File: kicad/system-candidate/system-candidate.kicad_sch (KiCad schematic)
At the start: 263 parts, among them J1 691137710002 2P 5.00mm, J2 Auxiliary 12V, J3 Differential audio, J301 T1_SECONDARY, J4 Control 2x4: 3V3 RESET FAULT 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, J401 START_BUTTON, J5 B2P-VH(LF)(SN), J6 GND braid solder bond - NO mo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, J7 B7B-XH-A(LF)(SN), J8 FAN 12V, K501 G6K-2F DC12, Q501 MMBT3904, Q502 MMBT3904, Q601 BCP56, Q602 BCP53, Q603 BSS138, Q701 BSS138, Q702 BSS138, Q703 BSS138, Q704 BSS138, Q705 BSS138, Q706 BSS138, Q707 AO3400A, U1 TPA3255DDV, U2 OPA1656ID, U3 OPA1656ID, U302 LM5164DDA, U303 TPS3700DDC, U401 LP2985-33, U402 TPS3808G33, U403 TPS3808G33, U404 TPS3808G33, U405 74LVC1G14, U406 74LVC2G74, U407 74LVC2G74, U408 74LVC1G32, U409 74LVC1G07, U410 74LVC1G08, U411 74LVC1G06, U412 TPS3700DDC, U413 TPS3700DDC, U414 TPS3808G33, U415 74LVC1G08, U416 TPS3808G33, U417 74LVC2G74, U418 74LVC1G32, U419 74LVC1G07, U501 TPS3700DDC, U502 TPS3700DDC, U503 TMUX6219, U504 TPS3700DDC

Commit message: fix(pcb): close routing and verify nominal fit
Correct TPA placement and TP127/R506 connectivity.\nPreserve OEM fit assumptions and explicit fabrication gates.\nSync documentation, renders, tasks and GitHub mirrors.\n\nValidate ERC/DRC/parity and 138 local tests.\n\nRefs #3, #7, #8, #10, #11
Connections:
- net INA_UV: no longer C503.1, D503.3 (K), R505.1, R517.2, TP127.1, U1.5 (INPUT_A)
- new net INPUT_A_AC: C503.1, D503.3 (K), R505.1, R517.2, TP127.1, U1.5 (INPUT_A)
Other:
- moved on the sheet: R107, R108, TP127

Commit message: fix(pcb): reconcile purchasing codes and add verified studio drafts
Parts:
- C14, C15: MPN UHE1J152MHD -> UHE1J681MHD
- J5: MPN 691137710002 -> B2P-VH(LF)(SN); Manufacturer Wurth Elektronik -> JST
- R101: MPN CRCW06031K00FKEA -> CRCW08051K00FKEA; Manufacturer (none) -> Vishay
- R102: MPN CRCW0603100KFKEA -> CRCW0805100KFKEA; Manufacturer (none) -> Vishay
- R310: MPN RG1608P-1053-B-T5 (TI Table 7-1); FSW 300 kHz -> RT0603BRD07100KL; Manufacturer (none) -> YAGEO

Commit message: fix(eda): align source notes and keep the whole board framed
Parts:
- C14, C15: Source Nichicon UHE CAT.8100M p.1/p.6: UHE1J152MHD 1500uF 63V D18 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 -> Nichicon UHE CAT.8100M: UHE1J681MHD 680uF 63V D12.5x40 P5; 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
- J5: Source WE WR-TBL1377 rev001.003 2021-07-30 p.1-2: pitch5.00 NOT5.0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 -> JST VH eVH-new p.3: B2P-VH(LF)(SN), 2 circuits, pitch3.96mm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

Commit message: feat(bom): close remaining 190 purchase selections
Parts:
- C1: SelectionNotes (none) -> WE WCAP-ATG5 rev1.0 2014-11-11 p.1: 470uF 35V D10 H16+1.5 P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; SelectionStatus Selected for engineering validation; NO procurement/release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 -> MPN SELECTED; supply/DFM/bench release pending
- C10, C11, C12, C13, C16, C17, C18, C19, C2, C20, C21, C24, C25, C28, C29, C3, C4, C5, C6, C7, C8, C9, J2: SelectionNotes (none) -> TI SLOU441 July2016 Table8 p.14-16; nominal package geometr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; SelectionStatus Selected for engineering validation; NO procurement/release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 -> MPN SELECTED; supply/DFM/bench release pending
- C107, C108: MPN TBD -> C0805C104K5RACTU; Manufacturer (none) -> KEMET; SelectionNotes (none) -> 100nF; 50V; X7R; 10%; 0805; SelectionStatus CANDIDATE; NOT PULSE/ESR/POWER-OFF/FIT QUALIFIED -> MPN SELECTED; supply/DFM/bench release pending
- C109: footprint Capacitor_THT:C_Rect_L7.2mm_W5.5mm_P5.00mm_FKS2_FKP2_MKS2_MKP2 -> Capacitor_THT:C_Rect_L7.2mm_W7.2mm_P5.00mm_FKS2_FKP2_MKS2_MKP2; MPN Film 2.2 uF >=63 V, P5 mm (WIMA MKS2 class); MPN at BOM -> MKS2C042201K00JSSD; Manufacturer (none) -> WIMA; SelectionNotes (none) -> 2.2uF; 63V; 5%; PET film; W7.2 H13 L7.2mm; pitch5; body foo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; SelectionStatus STUDY; passives/interfaces not selected -> MPN SELECTED; supply/DFM/bench release pending
- C14, C15: SelectionNotes (none) -> Nichicon UHE CAT.8100M: UHE1J681MHD 680uF 63V D12.5x40 P5; 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; SelectionStatus Selected for engineering validation; NO procurement/release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 -> MPN SELECTED; supply/DFM/bench release pending
- C201, C202: Manufacturer (none) -> Wurth Elektronik; SelectionNotes (none) -> 470uF; 35V; D10x16; pitch5; unchanged selected core capacit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; SelectionStatus CANDIDATE; NOT PULSE/ESR/POWER-OFF/FIT QUALIFIED -> MPN SELECTED; supply/DFM/bench release pending
- C203: Manufacturer (none) -> WIMA; SelectionNotes (none) -> 1uF; 63V; 5%; PP film; W11 H21 L7.2mm; pitch5; SelectionStatus CANDIDATE; NOT PULSE/ESR/POWER-OFF/FIT QUALIFIED -> MPN SELECTED; supply/DFM/bench release pending
- C22, C23, C26, C27: SelectionNotes (none) -> WIMA MKP2 03.26 p.38-39: 470nF 100V, W8.5 H14 L7.2 PCM5; J 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; SelectionStatus Selected for engineering validation; NO procurement/release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 -> MPN SELECTED; supply/DFM/bench release pending
- C301, C302: MPN Rubycon 63USC4700MEFCSN30X30 (LCSC C1498587): 4700 uF/63 V,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 -> 63USC4700MEFCSN30X30; Manufacturer (none) -> Rubycon; SelectionNotes (none) -> 4700uF; 63V; D30x30; pitch10; 3.49Arms/120Hz; total with C1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; SelectionStatus STUDY; passives/interfaces not selected -> MPN SELECTED; supply/DFM/bench release pending; Source D-021/D-020 captures; see docs/power-d021.md and docs/seq-d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 -> https://www.rubycon.co.jp/wp-content/uploads/catalog-alumin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
- C310, C311: MPN CGA6N3X7R2A225K230AB (TI Table 7-1) -> CGA6N3X7R2A225K230AB; Manufacturer (none) -> TDK; SelectionNotes (none) -> 2.2uF; 100V; X7R; 1210; TI Table7-1; effective capacitance 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; SelectionStatus STUDY; passives/interfaces not selected -> MPN SELECTED; supply/DFM/bench release pending
- C312: MPN GCM155R71H222KA37D (TI Table 7-1); 1.5-2.5 nF abs range -> GCM155R71H222KA37D; Manufacturer (none) -> Murata; SelectionNotes (none) -> 2.2nF; 50V; X7R; 0402; 10%; within TI bootstrap1.5-2.5nF at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; SelectionStatus STUDY; passives/interfaces not selected -> MPN SELECTED; supply/DFM/bench release pending
- C313: MPN CGA3E2X7R2A332K080AA (TI Table 7-1); CA -> CGA3E2X7R2A332K080AA; Manufacturer (none) -> TDK; SelectionNotes (none) -> 3.3nF; 100V; X7R; 0603; TI Table7-1; SelectionStatus STUDY; passives/interfaces not selected -> MPN SELECTED; supply/DFM/bench release pending
- C314: MPN C0603C560J5GACTU (TI Table 7-1); CB -> C0603C560J5GACTU; Manufacturer (none) -> KEMET; SelectionNotes (none) -> 56pF; 50V; C0G; 5%; 0603; TI Table7-1; SelectionStatus STUDY; passives/interfaces not selected -> MPN SELECTED; supply/DFM/bench release pending
- C315, C316: MPN TMK325B7226KMHT (TI Table 7-1) -> TMK325B7226KMHT; Manufacturer (none) -> Taiyo Yuden; SelectionNotes (none) -> 22uF; 25V; X7R; 1210; TI Table7-1; SelectionStatus STUDY; passives/interfaces not selected -> MPN SELECTED; supply/DFM/bench release pending
- C320: MPN TBD: X7R >=25 V (SBVS187G p.4 VDD bypass) -> C0603C104K5RACTU; Manufacturer (none) -> KEMET; SelectionNotes (none) -> 100nF; 50V; X7R; 10%; 0603; SelectionStatus STUDY; passives/interfaces not selected -> MPN SELECTED; supply/DFM/bench release pending
- C401: MPN TBD: X7R >=25 V; CIN >=1 uF (SLVS522S Table 4-1) -> GRM188R71E105KA12D; Manufacturer (none) -> Murata; SelectionNotes (none) -> 1uF; 25V; X7R; 10%; 0603; C401 input at12V: bias derating a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; SelectionStatus STUDY; passives/interfaces not selected -> MPN SELECTED; supply/DFM/bench release pending
- C402: MPN TBD: X7R; CBYPASS 10 nF (SLVS522S) -> 06031C103KAT2A; Manufacturer (none) -> KYOCERA AVX; SelectionNotes (none) -> 10nF; 100V; X7R; 10%; 0603; same as selected C25/C29; SelectionStatus STUDY; passives/interfaces not selected -> MPN SELECTED; supply/DFM/bench release pending
- C403: MPN TBD: X7R, >=1 uF effective, ESR <=1 ohm new die -> GRM188Z71C225KE43D; Manufacturer (none) -> Murata; SelectionNotes (none) -> 2.2uF; 16V; X7R(Murata); 10%; 0603; TI EVM C118; LP2985 out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; SelectionStatus STUDY; passives/interfaces not selected -> MPN SELECTED; supply/DFM/bench release pending
- C404: MPN TBD: C0G/X7R low leakage; CT 180 nF => 0.62-1.44 s -> GRM188R71E184KA88D; Manufacturer (none) -> Murata; SelectionNotes (none) -> 180nF; 25V; X7R; 10%; 0603; CT at low bias; specified timin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; SelectionStatus STUDY; passives/interfaces not selected -> MPN SELECTED; supply/DFM/bench release pending
- C405: MPN TBD: X7R; release tau ~110 ms -> GRM188R71E105KA12D; Manufacturer (none) -> Murata; SelectionNotes (none) -> 1uF; 25V; X7R; 10%; 0603; C401 input at12V: bias derating a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; SelectionStatus STUDY; passives/interfaces not selected -> MPN SELECTED; supply/DFM/bench release pending
- C406: MPN TBD: X7R >=10 V; U402 -> C0603C104K5RACTU; Manufacturer (none) -> KEMET; SelectionNotes (none) -> 100nF; 50V; X7R; 10%; 0603; SelectionStatus STUDY; passives/interfaces not selected -> MPN SELECTED; supply/DFM/bench release pending
- C407: MPN TBD: X7R >=10 V; U403 -> C0603C104K5RACTU; Manufacturer (none) -> KEMET; SelectionNotes (none) -> 100nF; 50V; X7R; 10%; 0603; SelectionStatus STUDY; passives/interfaces not selected -> MPN SELECTED; supply/DFM/bench release pending
- C408: MPN TBD: X7R >=10 V; U404 -> C0603C104K5RACTU; Manufacturer (none) -> KEMET; SelectionNotes (none) -> 100nF; 50V; X7R; 10%; 0603; SelectionStatus STUDY; passives/interfaces not selected -> MPN SELECTED; supply/DFM/bench release pending
- C409: MPN TBD: X7R >=10 V; U405 -> C0603C104K5RACTU; Manufacturer (none) -> KEMET; SelectionNotes (none) -> 100nF; 50V; X7R; 10%; 0603; SelectionStatus STUDY; passives/interfaces not selected -> MPN SELECTED; supply/DFM/bench release pending
- C410: MPN TBD: X7R >=10 V; U406 -> C0603C104K5RACTU; Manufacturer (none) -> KEMET; SelectionNotes (none) -> 100nF; 50V; X7R; 10%; 0603; SelectionStatus STUDY; passives/interfaces not selected -> MPN SELECTED; supply/DFM/bench release pending
- C411: MPN TBD: X7R >=10 V; U407 -> C0603C104K5RACTU; Manufacturer (none) -> KEMET; SelectionNotes (none) -> 100nF; 50V; X7R; 10%; 0603; SelectionStatus STUDY; passives/interfaces not selected -> MPN SELECTED; supply/DFM/bench release pending
- C412: MPN TBD: X7R >=10 V; U408 -> C0603C104K5RACTU; Manufacturer (none) -> KEMET; SelectionNotes (none) -> 100nF; 50V; X7R; 10%; 0603; SelectionStatus STUDY; passives/interfaces not selected -> MPN SELECTED; supply/DFM/bench release pending
- C413: MPN TBD: X7R >=10 V; U409 -> C0603C104K5RACTU; Manufacturer (none) -> KEMET; SelectionNotes (none) -> 100nF; 50V; X7R; 10%; 0603; SelectionStatus STUDY; passives/interfaces not selected -> MPN SELECTED; supply/DFM/bench release pending
- C414: MPN TBD: X7R >=10 V; U410 -> C0603C104K5RACTU; Manufacturer (none) -> KEMET; SelectionNotes (none) -> 100nF; 50V; X7R; 10%; 0603; SelectionStatus STUDY; passives/interfaces not selected -> MPN SELECTED; supply/DFM/bench release pending
- C415: MPN TBD: X7R >=10 V; U411 -> C0603C104K5RACTU; Manufacturer (none) -> KEMET; SelectionNotes (none) -> 100nF; 50V; X7R; 10%; 0603; SelectionStatus STUDY; passives/interfaces not selected -> MPN SELECTED; supply/DFM/bench release pending
- C416: MPN TBD: X7R >=25 V; U412 VDD -> C0603C104K5RACTU; Manufacturer (none) -> KEMET; SelectionNotes (none) -> 100nF; 50V; X7R; 10%; 0603; SelectionStatus STUDY; passives/interfaces not selected -> MPN SELECTED; supply/DFM/bench release pending
- C417: MPN TBD: X7R >=25 V; U413 VDD -> C0603C104K5RACTU; Manufacturer (none) -> KEMET; SelectionNotes (none) -> 100nF; 50V; X7R; 10%; 0603; SelectionStatus STUDY; passives/interfaces not selected -> MPN SELECTED; supply/DFM/bench release pending
- C418: MPN TBD: X7R >=10 V; U414 -> C0603C104K5RACTU; Manufacturer (none) -> KEMET; SelectionNotes (none) -> 100nF; 50V; X7R; 10%; 0603; SelectionStatus STUDY; passives/interfaces not selected -> MPN SELECTED; supply/DFM/bench release pending
- C419: MPN TBD: X7R >=10 V; U415 -> C0603C104K5RACTU; Manufacturer (none) -> KEMET; SelectionNotes (none) -> 100nF; 50V; X7R; 10%; 0603; SelectionStatus STUDY; passives/interfaces not selected -> MPN SELECTED; supply/DFM/bench release pending
- C420: MPN TBD: X7R >=10 V; U416 -> C0603C104K5RACTU; Manufacturer (none) -> KEMET; SelectionNotes (none) -> 100nF; 50V; X7R; 10%; 0603; SelectionStatus STUDY; passives/interfaces not selected -> MPN SELECTED; supply/DFM/bench release pending
- C421: MPN TBD: X7R >=10 V; U417 -> C0603C104K5RACTU; Manufacturer (none) -> KEMET; SelectionNotes (none) -> 100nF; 50V; X7R; 10%; 0603; SelectionStatus STUDY; passives/interfaces not selected -> MPN SELECTED; supply/DFM/bench release pending
- C422: MPN TBD: X7R >=10 V; U418 -> C0603C104K5RACTU; Manufacturer (none) -> KEMET; SelectionNotes (none) -> 100nF; 50V; X7R; 10%; 0603; SelectionStatus STUDY; passives/interfaces not selected -> MPN SELECTED; supply/DFM/bench release pending
- C423: MPN TBD: X7R >=10 V; U419 -> C0603C104K5RACTU; Manufacturer (none) -> KEMET; SelectionNotes (none) -> 100nF; 50V; X7R; 10%; 0603; SelectionStatus STUDY; passives/interfaces not selected -> MPN SELECTED; supply/DFM/bench release pending
- C503, C504: MPN TBD: C0G/NP0 >=50 V -> C0603C472J5GACTU; Manufacturer (none) -> KEMET; SelectionNotes (none) -> 4.7nF; 50V; C0G; 5%; 0603; SelectionStatus STUDY; passives/interfaces not selected -> MPN SELECTED; supply/DFM/bench release pending
- C505: MPN TBD: X7R >=25 V; U503 VDD (SCDS420E Table 4-1) -> C0603C104K5RACTU; Manufacturer (none) -> KEMET; SelectionNotes (none) -> 100nF; 50V; X7R; 10%; 0603; SelectionStatus STUDY; passives/interfaces not selected -> MPN SELECTED; supply/DFM/bench release pending
- C506: MPN TBD: X7R >=25 V; U501 VDD -> C0603C104K5RACTU; Manufacturer (none) -> KEMET; SelectionNotes (none) -> 100nF; 50V; X7R; 10%; 0603; SelectionStatus STUDY; passives/interfaces not selected -> MPN SELECTED; supply/DFM/bench release pending
- C507: MPN TBD: X7R >=25 V; U502 VDD -> C0603C104K5RACTU; Manufacturer (none) -> KEMET; SelectionNotes (none) -> 100nF; 50V; X7R; 10%; 0603; SelectionStatus STUDY; passives/interfaces not selected -> MPN SELECTED; supply/DFM/bench release pending
- C508: MPN TBD: X7R >=25 V; U504 VDD -> C0603C104K5RACTU; Manufacturer (none) -> KEMET; SelectionNotes (none) -> 100nF; 50V; X7R; 10%; 0603; SelectionStatus STUDY; passives/interfaces not selected -> MPN SELECTED; supply/DFM/bench release pending
- C509, C511: MPN TBD: X7R >=16 V; UV tap filter -> C0603C334K4RACTU; Manufacturer (none) -> KEMET; SelectionNotes (none) -> 330nF; 16V; X7R; 10%; 0603; window tap <1V; SelectionStatus STUDY; passives/interfaces not selected -> MPN SELECTED; supply/DFM/bench release pending
- C510, C512: MPN TBD: X7R >=16 V; OV tap filter -> CC0603KRX7R8BB684; Manufacturer (none) -> YAGEO; SelectionNotes (none) -> 680nF; 25V; X7R; 10%; 0603; window tap <1V; SelectionStatus STUDY; passives/interfaces not selected -> MPN SELECTED; supply/DFM/bench release pending
- C601, C604: MPN X7R 1206 >=25 V; MPN at BOM -> C3216X7R1E106K160AB; Manufacturer (none) -> TDK; SelectionNotes (none) -> 10uF; 25V; X7R; 10%; 1206; OEM +/-15V interface bypass; SelectionStatus STUDY; passives/interfaces not selected -> MPN SELECTED; supply/DFM/bench release pending
- C602, C605: MPN X7R 0603 50 V -> C0603C104K5RACTU; Manufacturer (none) -> KEMET; SelectionNotes (none) -> 100nF; 50V; X7R; 10%; 0603; SelectionStatus STUDY; passives/interfaces not selected -> MPN SELECTED; supply/DFM/bench release pending
- C603: MPN Nichicon UHE1J121MPD 120 uF/63 V 8x20 (CAT.8100M) -> UHE1J121MPD; Manufacturer (none) -> Nichicon; SelectionNotes (none) -> 120uF; 63V; D8x20; pitch3.5; SelectionStatus STUDY; passives/interfaces not selected -> MPN SELECTED; supply/DFM/bench release pending
- D201: Manufacturer (none) -> Vishay; SelectionNotes (none) -> 1000V; 1A; DO41 axial; polarity per footprint cathode1; SelectionStatus CANDIDATE; NOT PULSE/ESR/POWER-OFF/FIT QUALIFIED -> MPN SELECTED; supply/DFM/bench release pending
- D301, D302: MPN P600J (Diodes Inc./Vishay), R-6 axial: 600 V, 6 A, IFSM 400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 -> P600J-E3/54; Manufacturer (none) -> Vishay; SelectionNotes (none) -> 600V; 6A; IFSM400A; P600/R6 axial; CT rectifier; manual lea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; SelectionStatus STUDY; passives/interfaces not selected -> MPN SELECTED; supply/DFM/bench release pending
- D303: MPN Littelfuse SMCJ51A: VWM 51.0 V, Vc 82.4 V @IPP 18.2 A, PPP 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 -> SMCJ51A; Manufacturer (none) -> Littelfuse; SelectionNotes (none) -> 51V standoff; 1500W10/1000us; Vclamp82.4V; not sustained ra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; SelectionStatus STUDY; passives/interfaces not selected -> MPN SELECTED; supply/DFM/bench release pending
- D501: MPN 1N4148W-7-F (Diodes DS30086) -> 1N4148W-7-F; Manufacturer (none) -> Diodes Incorporated; SelectionNotes (none) -> SOD123; fast signal diode; SelectionStatus STUDY; passives/interfaces not selected -> MPN SELECTED; supply/DFM/bench release pending
- D502: MPN BZT52C15-7-F (Diodes DS18004): 13.8-15.6 V; faster release -> BZT52C15-7-F; Manufacturer (none) -> Diodes Incorporated; SelectionNotes (none) -> 15V; SOD123; 13.8-15.6V at5mA; SelectionStatus STUDY; passives/interfaces not selected -> MPN SELECTED; supply/DFM/bench release pending
- D503, D504: MPN BAT54-7-F (Diodes DS11005 Rev.34) -> BAT54-7-F; Manufacturer (none) -> Diodes Incorporated; SelectionNotes (none) -> 30V; SOT23; single Schottky; pin1 A pin3 K; SelectionStatus STUDY; passives/interfaces not selected -> MPN SELECTED; supply/DFM/bench release pending
- D601: MPN Diodes BZT52C16 (DS18004): 15.3-17.1 V @5 mA -> BZT52C16-7-F; Manufacturer (none) -> Diodes Incorporated; SelectionNotes (none) -> 16V; SOD123; 15.3-17.1V at5mA; SelectionStatus STUDY; passives/interfaces not selected -> MPN SELECTED; supply/DFM/bench release pending
- D602, D603: MPN S1M 1000 V 1 A SMA (Vishay/onsemi); light load -> S1M-E3/61T; Manufacturer (none) -> Vishay; SelectionNotes (none) -> 1000V; 1A; SMA/DO214AC; cathode1; light-load rectification/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; SelectionStatus STUDY; passives/interfaces not selected -> MPN SELECTED; supply/DFM/bench release pending
- D604: MPN Diodes BZT52C16 (DS18004) -> BZT52C16-7-F; Manufacturer (none) -> Diodes Incorporated; SelectionNotes (none) -> 16V; SOD123; 15.3-17.1V at5mA; SelectionStatus STUDY; passives/interfaces not selected -> MPN SELECTED; supply/DFM/bench release pending
- D701, D702, D703, D704, D705, D706: MPN Green 0805 LED (e.g. Lite-On LTST-C171GKT) -> LTST-C171GKT; Manufacturer (none) -> Lite-On; SelectionNotes (none) -> green LED; 0805; polarity pin1 cathode; resistive current l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; SelectionStatus STUDY; passives/interfaces not selected -> MPN SELECTED; supply/DFM/bench release pending
- D707: MPN S1M flyback across the fan -> S1M-E3/61T; Manufacturer (none) -> Vishay; SelectionNotes (none) -> 1000V; 1A; SMA/DO214AC; cathode1; light-load rectification/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; SelectionStatus STUDY; passives/interfaces not selected -> MPN SELECTED; supply/DFM/bench release pending
- F301: MPN Littelfuse 02186.3MXP, 218 series T 6.3 A 5x20 mm, in Schur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 -> 0031.8201; Manufacturer (none) -> Schurter; SelectionNotes (none) -> PCB fuse holder for5x20; P22.5mm; separate fuse F301-FUSE i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; SelectionStatus STUDY; passives/interfaces not selected -> MPN SELECTED; supply/DFM/bench release pending
- J1: SelectionNotes (none) -> WE WR-TBL1377 rev001.003 2021-07-30 p.1-2: pitch5.00 NOT5.0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; SelectionStatus Selected for engineering validation; NO procurement/release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 -> MPN SELECTED; supply/DFM/bench release pending
- J301: MPN JST B3P-VH(LF)(SN) header 3 pos 3.96 mm; mates OEM T1 harne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 -> B3P-VH(LF)(SN); Manufacturer (none) -> JST; SelectionNotes (none) -> 3way; 3.96mm; CT T1 OEM harness, never bridge red-red; SelectionStatus STUDY; passives/interfaces not selected -> MPN SELECTED; supply/DFM/bench release pending
- J401: MPN TBD: panel momentary switch harness; location/mechanics not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 -> PBC02SAAN; Manufacturer (none) -> Sullins Connector Solutions; SelectionNotes (none) -> 2pin straight header; P2.54mm; external momentary NO switch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; SelectionStatus STUDY; passives/interfaces not selected -> MPN SELECTED; supply/DFM/bench release pending
- J5: SelectionNotes (none) -> JST VH eVH-new p.3: B2P-VH(LF)(SN), 2 circuits, pitch3.96mm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; SelectionStatus Selected for engineering validation; NO procurement/release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 -> MPN SELECTED; supply/DFM/bench release pending
- J7: MPN JST B7B-XH-A(LF)(SN), 2.5 mm: mates OEM 7-way preamp harnes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 -> B7B-XH-A(LF)(SN); Manufacturer (none) -> JST; SelectionNotes (none) -> 7way; 2.5mm; mates OEM P101 harness, pinout per current des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; SelectionStatus STUDY; passives/interfaces not selected -> MPN SELECTED; supply/DFM/bench release pending
- J8: MPN JST B2B-XH-A(LF)(SN); fan <= 200 mA -> B2B-XH-A(LF)(SN); Manufacturer (none) -> JST; SelectionNotes (none) -> 2way; 2.5mm; fan<=200mA; SelectionStatus STUDY; passives/interfaces not selected -> MPN SELECTED; supply/DFM/bench release pending
- JP701: MPN 2.54 mm header + jumper: 1-2 ON, 2-3 OTW -> PBC03SAAN; Manufacturer (none) -> Sullins Connector Solutions; SelectionNotes (none) -> 3pin straight header; P2.54mm; shunt separate accessory; 1-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; SelectionStatus STUDY; passives/interfaces not selected -> MPN SELECTED; supply/DFM/bench release pending
- K501: MPN G6K-2F DC12 (Omron K106-E1-11 p.2-3: 1315 ohm, 3 ms operate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 -> G6K-2F DC12; Manufacturer (none) -> Omron; SelectionNotes (none) -> 12V monostable DPDT; SMD; 1315ohm; operate/release3ms max; 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; SelectionStatus STUDY; passives/interfaces not selected -> MPN SELECTED; supply/DFM/bench release pending
- L1, L2: SelectionNotes (none) -> WE 006.000 2025-07-08 p.1: 10uH/16A/22A typ/8.76mOhm max; s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; SelectionStatus Selected for engineering validation; NO procurement/release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 -> MPN SELECTED; supply/DFM/bench release pending
- L301: MPN MSS1246T-683MLB (TI Table 7-1); Isat above 1.5 A limit -> MSS1246T-683MLC; Manufacturer (none) -> Coilcraft; SelectionNotes (none) -> 68uH; 20%; Irms1.8A; Isat2.26A at10% drop; 12x12x4.6mm; cur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; SelectionStatus STUDY; passives/interfaces not selected -> MPN SELECTED; supply/DFM/bench release pending
- Q501: MPN MMBT3904-7-F (Diodes DS30036): VCEsat <=0.2 V at 10 mA/1 mA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 -> MMBT3904-7-F; Manufacturer (none) -> Diodes Incorporated; SelectionNotes (none) -> NPN;40V;SOT23; pin1B2E3C; VCEsat0.2V max10mA/1mA; SelectionStatus STUDY; passives/interfaces not selected -> MPN SELECTED; supply/DFM/bench release pending
- Q502: MPN MMBT3904-7-F (Diodes DS30036); unmute pull-down -> MMBT3904-7-F; Manufacturer (none) -> Diodes Incorporated; SelectionNotes (none) -> NPN;40V;SOT23; pin1B2E3C; VCEsat0.2V max10mA/1mA; SelectionStatus STUDY; passives/interfaces not selected -> MPN SELECTED; supply/DFM/bench release pending
- Q601: MPN onsemi BCP56T1G: 80 V, 1 A, SOT-223 -> BCP56T1G; Manufacturer (none) -> onsemi; SelectionNotes (none) -> 80V;1A; SOT223; pin1B2C3E tab2; NPN; SelectionStatus STUDY; passives/interfaces not selected -> MPN SELECTED; supply/DFM/bench release pending
- Q602: MPN onsemi BCP53T1G: -80 V, -1 A, SOT-223 -> BCP53T1G; Manufacturer (none) -> onsemi; SelectionNotes (none) -> -80V;-1A; SOT223; pin1B2C3E tab2; PNP; SelectionStatus STUDY; passives/interfaces not selected -> MPN SELECTED; supply/DFM/bench release pending
- Q603: MPN onsemi BSS138: gate on CLIP_OTW, no DC load on the TPA pin -> BSS138LT1G; Manufacturer (none) -> onsemi; SelectionNotes (none) -> 50V N-MOS; SOT23; pin1G2S3D; SelectionStatus STUDY; passives/interfaces not selected -> MPN SELECTED; supply/DFM/bench release pending
- Q701, Q702, Q703, Q704, Q705, Q706: MPN onsemi BSS138 -> BSS138LT1G; Manufacturer (none) -> onsemi; SelectionNotes (none) -> 50V N-MOS; SOT23; pin1G2S3D; SelectionStatus STUDY; passives/interfaces not selected -> MPN SELECTED; supply/DFM/bench release pending
- Q707: MPN AOS AO3400A -> AO3400A; Manufacturer (none) -> Alpha & Omega Semiconductor; SelectionNotes (none) -> 30V N-MOS;SOT23;pin1G2S3D; fan<=200mA; SelectionStatus STUDY; passives/interfaces not selected -> MPN SELECTED; supply/DFM/bench release pending
- R1, R2, R3, R4, R5, R6, R9: SelectionNotes (none) -> Vishay D/CRCW e3 doc20035: 0603 0.1W, 1206 0.25W and orderi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; SelectionStatus Selected for engineering validation; NO procurement/release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 -> MPN SELECTED; supply/DFM/bench release pending
- R101, R102: SelectionNotes (none) -> D-020 candidate; primary parts/landpattern refs in docs/int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; SelectionStatus CANDIDATE; NOT PULSE/ESR/POWER-OFF/FIT QUALIFIED -> MPN SELECTED; supply/DFM/bench release pending
- R107, R108: MPN TBD -> CRCW080510K0FKEA; Manufacturer (none) -> Vishay; SelectionNotes (none) -> 10k; 1%; 0805; 0.125W; 150V; SelectionStatus CANDIDATE; NOT PULSE/ESR/POWER-OFF/FIT QUALIFIED -> MPN SELECTED; supply/DFM/bench release pending
- R110: MPN 0603 1 % thin film; U2A gain 1+8.87k/10k = 1.887 -> RT0603BRD078K87L; Manufacturer (none) -> YAGEO; SelectionNotes (none) -> 8.87k ohm notation; 0.1%; 25 ppm/K; 0603; 0.1W; 75V; SelectionStatus STUDY; passives/interfaces not selected -> MPN SELECTED; supply/DFM/bench release pending
- R111: MPN 0603 1 % thin film -> RT0603BRD0710KL; Manufacturer (none) -> YAGEO; SelectionNotes (none) -> 10k ohm notation; 0.1%; 25 ppm/K; 0603; 0.1W; 75V; SelectionStatus STUDY; passives/interfaces not selected -> MPN SELECTED; supply/DFM/bench release pending
- R201: Manufacturer (none) -> Vishay; SelectionNotes (none) -> 15 ohm; 3W; axial vertical; insulated lead and body spacing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; SelectionStatus CANDIDATE; NOT PULSE/ESR/POWER-OFF/FIT QUALIFIED -> MPN SELECTED; supply/DFM/bench release pending
- R202, R203: Manufacturer (none) -> Vishay; SelectionNotes (none) -> 0.1%; 25ppm/K; custom IPC reflow land pattern per Vishay 28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; SelectionStatus CANDIDATE; NOT PULSE/ESR/POWER-OFF/FIT QUALIFIED -> MPN SELECTED; supply/DFM/bench release pending
- R204, R205, R206, R207: Manufacturer (none) -> Vishay; SelectionNotes (none) -> 75; 1%; 1206; 0.25W; 200V; SelectionStatus CANDIDATE; NOT PULSE/ESR/POWER-OFF/FIT QUALIFIED -> MPN SELECTED; supply/DFM/bench release pending
- R301: MPN TBD: >=1 W continuous at 50 V (0.53 W), >=100 V -> PR02000204701JA100; Manufacturer (none) -> Vishay; SelectionNotes (none) -> 4.7k; 5%; 2W Cu leads; 500V; axial L12 max/D4.5 max; form l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; SelectionStatus STUDY; passives/interfaces not selected -> MPN SELECTED; supply/DFM/bench release pending
- R310: SelectionNotes (none) -> D-021/D-020 captures; see docs/power-d021.md and docs/seq-d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; SelectionStatus STUDY; passives/interfaces not selected -> MPN SELECTED; supply/DFM/bench release pending
- R311: MPN TBD: TI Table 7-1 lists RT0603BRD07448KL (448k) against val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 -> RT0603BRD07453KL; Manufacturer (none) -> YAGEO; SelectionNotes (none) -> 453k ohm notation; 0.1%; 25 ppm/K; 0603; 0.1W; 75V; SelectionStatus STUDY; passives/interfaces not selected -> MPN SELECTED; supply/DFM/bench release pending
- R312: MPN RG1608P-4992-B-T5 (TI Table 7-1) -> RG1608P-4992-B-T5; Manufacturer (none) -> Susumu; SelectionNotes (none) -> 49.9k; 0.1%; 25ppm/K; 0603; TI LM5164 Table7-1; SelectionStatus STUDY; passives/interfaces not selected -> MPN SELECTED; supply/DFM/bench release pending
- R313: MPN RT0603BRD07453KL (TI Table 7-1); RA type-3 ripple -> RT0603BRD07453KL; Manufacturer (none) -> YAGEO; SelectionNotes (none) -> 453k ohm notation; 0.1%; 25 ppm/K; 0603; 0.1W; 75V; SelectionStatus STUDY; passives/interfaces not selected -> MPN SELECTED; supply/DFM/bench release pending
- R320: MPN TBD: 0.1 %, <=25 ppm/K, >=100 V working (sees ~50 V) -> RT1206BRD07931KL; Manufacturer (none) -> YAGEO; SelectionNotes (none) -> 931k ohm notation; 0.1%; 25 ppm/K; 1206; 0.25W; 200V; SelectionStatus STUDY; passives/interfaces not selected -> MPN SELECTED; supply/DFM/bench release pending
- R321: MPN TBD: 0.1 %, <=25 ppm/K -> RT0603BRD076K04L; Manufacturer (none) -> YAGEO; SelectionNotes (none) -> 6.04k ohm notation; 0.1%; 25 ppm/K; 0603; 0.1W; 75V; SelectionStatus STUDY; passives/interfaces not selected -> MPN SELECTED; supply/DFM/bench release pending
- R322: MPN TBD: 0.1 %, <=25 ppm/K -> RT0603BRD077K32L; Manufacturer (none) -> YAGEO; SelectionNotes (none) -> 7.32k ohm notation; 0.1%; 25 ppm/K; 0603; 0.1W; 75V; SelectionStatus STUDY; passives/interfaces not selected -> MPN SELECTED; supply/DFM/bench release pending
- R323: MPN TBD: pull-up to SEQ_3V3 (seq-d020 LP2985); <=14 V LM5164 PG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 -> CRCW0603100KFKEA; Manufacturer (none) -> Vishay; SelectionNotes (none) -> 100k; 1%; 0603; 0.1W; 75V; SelectionStatus STUDY; passives/interfaces not selected -> MPN SELECTED; supply/DFM/bench release pending
- R401: MPN TBD: 1 %; CT to VDD 40-200k => 180/300/420 ms -> CRCW0603100KFKEA; Manufacturer (none) -> Vishay; SelectionNotes (none) -> 100k; 1%; 0603; 0.1W; 75V; SelectionStatus STUDY; passives/interfaces not selected -> MPN SELECTED; supply/DFM/bench release pending
- R402: MPN TBD: RESET pull-up 10k-1M (SBVS050N Table 5-1) -> CRCW0603100KFKEA; Manufacturer (none) -> Vishay; SelectionNotes (none) -> 100k; 1%; 0603; 0.1W; 75V; SelectionStatus STUDY; passives/interfaces not selected -> MPN SELECTED; supply/DFM/bench release pending
- R403: MPN TBD: 1 %; CT to VDD -> CRCW0603100KFKEA; Manufacturer (none) -> Vishay; SelectionNotes (none) -> 100k; 1%; 0603; 0.1W; 75V; SelectionStatus STUDY; passives/interfaces not selected -> MPN SELECTED; supply/DFM/bench release pending
- R404, R405, R428, R430: MPN TBD: RESET pull-up -> CRCW0603100KFKEA; Manufacturer (none) -> Vishay; SelectionNotes (none) -> 100k; 1%; 0603; 0.1W; 75V; SelectionStatus STUDY; passives/interfaces not selected -> MPN SELECTED; supply/DFM/bench release pending
- R406: MPN TBD: button pull-up -> CRCW0603100KFKEA; Manufacturer (none) -> Vishay; SelectionNotes (none) -> 100k; 1%; 0603; 0.1W; 75V; SelectionStatus STUDY; passives/interfaces not selected -> MPN SELECTED; supply/DFM/bench release pending
- R407: MPN TBD: debounce series; press tau 10 ms -> CRCW060310K0FKEA; Manufacturer (none) -> Vishay; SelectionNotes (none) -> 10k; 1%; 0603; 0.1W; 75V; SelectionStatus STUDY; passives/interfaces not selected -> MPN SELECTED; supply/DFM/bench release pending
- R408: MPN TBD: series to TPA RESET; with R9 4.7k gives >=2.6 V (VIH 1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 -> CRCW06031K00FKEA; Manufacturer (none) -> Vishay; SelectionNotes (none) -> 1k; 1%; 0603; 0.1W; 75V; SelectionStatus STUDY; passives/interfaces not selected -> MPN SELECTED; supply/DFM/bench release pending
- R420, R422, R426: MPN TBD: 0.1 %, <=25 ppm/K -> RT0603BRD071ML; Manufacturer (none) -> YAGEO; SelectionNotes (none) -> 1M ohm notation; 0.1%; 25 ppm/K; 0603; 0.1W; 75V; SelectionStatus STUDY; passives/interfaces not selected -> MPN SELECTED; supply/DFM/bench release pending
- R421: MPN TBD: 0.1 %, <=25 ppm/K -> RT0603BRD0746K4L; Manufacturer (none) -> YAGEO; SelectionNotes (none) -> 46.4k ohm notation; 0.1%; 25 ppm/K; 0603; 0.1W; 75V; SelectionStatus STUDY; passives/interfaces not selected -> MPN SELECTED; supply/DFM/bench release pending
- R423: MPN TBD: 0.1 %, <=25 ppm/K -> RT0603BRD0730K1L; Manufacturer (none) -> YAGEO; SelectionNotes (none) -> 30.1k ohm notation; 0.1%; 25 ppm/K; 0603; 0.1W; 75V; SelectionStatus STUDY; passives/interfaces not selected -> MPN SELECTED; supply/DFM/bench release pending
- R424: MPN TBD: 0.1 %, <=25 ppm/K -> RT0603BRD07909KL; Manufacturer (none) -> YAGEO; SelectionNotes (none) -> 909k ohm notation; 0.1%; 25 ppm/K; 0603; 0.1W; 75V; SelectionStatus STUDY; passives/interfaces not selected -> MPN SELECTED; supply/DFM/bench release pending
- R425: MPN TBD: 0.1 %, <=25 ppm/K -> RT0603BRD07101KL; Manufacturer (none) -> YAGEO; SelectionNotes (none) -> 101k ohm notation; 0.1%; 25 ppm/K; 0603; 0.1W; 75V; SelectionStatus STUDY; passives/interfaces not selected -> MPN SELECTED; supply/DFM/bench release pending
- R427: MPN TBD: 0.1 %, <=25 ppm/K -> RT0603BRD0764K9L; Manufacturer (none) -> YAGEO; SelectionNotes (none) -> 64.9k ohm notation; 0.1%; 25 ppm/K; 0603; 0.1W; 75V; SelectionStatus STUDY; passives/interfaces not selected -> MPN SELECTED; supply/DFM/bench release pending
- R429: MPN TBD: DC_OK pull-up (open-drain from iso-d019 U501/U502) -> CRCW0603100KFKEA; Manufacturer (none) -> Vishay; SelectionNotes (none) -> 100k; 1%; 0603; 0.1W; 75V; SelectionStatus STUDY; passives/interfaces not selected -> MPN SELECTED; supply/DFM/bench release pending
- R501: MPN TBD: 1 %; IB >=1.0 mA from 3.3 V (VBEsat 0.85 V max) -> CRCW06032K20FKEA; Manufacturer (none) -> Vishay; SelectionNotes (none) -> 2.2k; 1%; 0603; 0.1W; 75V; SelectionStatus STUDY; passives/interfaces not selected -> MPN SELECTED; supply/DFM/bench release pending
- R502: MPN TBD: base pull-down, relay off without logic -> CRCW0603100KFKEA; Manufacturer (none) -> Vishay; SelectionNotes (none) -> 100k; 1%; 0603; 0.1W; 75V; SelectionStatus STUDY; passives/interfaces not selected -> MPN SELECTED; supply/DFM/bench release pending
- R503, R504: MPN TBD: 1 %, >=0.1 W; tau 10 ms with 10 uF -> CRCW06031K00FKEA; Manufacturer (none) -> Vishay; SelectionNotes (none) -> 1k; 1%; 0603; 0.1W; 75V; SelectionStatus STUDY; passives/interfaces not selected -> MPN SELECTED; supply/DFM/bench release pending
- R505, R508: MPN TBD: 0.1 %, <=25 ppm/K; pin DC window and return -> RT0603BRD07787KL; Manufacturer (none) -> YAGEO; SelectionNotes (none) -> 787k ohm notation; 0.1%; 25 ppm/K; 0603; 0.1W; 75V; SelectionStatus STUDY; passives/interfaces not selected -> MPN SELECTED; supply/DFM/bench release pending
- R506, R509: MPN TBD: 0.1 %, <=25 ppm/K; pin DC window and return -> RT0603BRD07115KL; Manufacturer (none) -> YAGEO; SelectionNotes (none) -> 115k ohm notation; 0.1%; 25 ppm/K; 0603; 0.1W; 75V; SelectionStatus STUDY; passives/interfaces not selected -> MPN SELECTED; supply/DFM/bench release pending
- R507, R510: MPN TBD: 0.1 %, <=25 ppm/K; pin DC window and return -> RT0603BRD0778K7L; Manufacturer (none) -> YAGEO; SelectionNotes (none) -> 78.7k ohm notation; 0.1%; 25 ppm/K; 0603; 0.1W; 75V; SelectionStatus STUDY; passives/interfaces not selected -> MPN SELECTED; supply/DFM/bench release pending
- R511: MPN TBD: EN pull-up to ANALOG_12V (default muted) -> CRCW0603100KFKEA; Manufacturer (none) -> Vishay; SelectionNotes (none) -> 100k; 1%; 0603; 0.1W; 75V; SelectionStatus STUDY; passives/interfaces not selected -> MPN SELECTED; supply/DFM/bench release pending
- R512: MPN TBD: 1 % -> CRCW060310K0FKEA; Manufacturer (none) -> Vishay; SelectionNotes (none) -> 10k; 1%; 0603; 0.1W; 75V; SelectionStatus STUDY; passives/interfaces not selected -> MPN SELECTED; supply/DFM/bench release pending
- R513: MPN TBD: base pull-down, muted without logic -> CRCW0603100KFKEA; Manufacturer (none) -> Vishay; SelectionNotes (none) -> 100k; 1%; 0603; 0.1W; 75V; SelectionStatus STUDY; passives/interfaces not selected -> MPN SELECTED; supply/DFM/bench release pending
- R514: MPN TBD: 0.1 %, <=25 ppm/K; AUX window -> RT0603BRD07357KL; Manufacturer (none) -> YAGEO; SelectionNotes (none) -> 357k ohm notation; 0.1%; 25 ppm/K; 0603; 0.1W; 75V; SelectionStatus STUDY; passives/interfaces not selected -> MPN SELECTED; supply/DFM/bench release pending
- R515: MPN TBD: 0.1 %, <=25 ppm/K; AUX window -> RT0603BRD071K5L; Manufacturer (none) -> YAGEO; SelectionNotes (none) -> 1.5k ohm notation; 0.1%; 25 ppm/K; 0603; 0.1W; 75V; SelectionStatus STUDY; passives/interfaces not selected -> MPN SELECTED; supply/DFM/bench release pending
- R516: MPN TBD: 0.1 %, <=25 ppm/K; AUX window -> RT0603BRD0711K5L; Manufacturer (none) -> YAGEO; SelectionNotes (none) -> 11.5k ohm notation; 0.1%; 25 ppm/K; 0603; 0.1W; 75V; SelectionStatus STUDY; passives/interfaces not selected -> MPN SELECTED; supply/DFM/bench release pending
- R517, R518: MPN TBD: 1 %, thin film; RIN 10/20/40k => -2.48/-1.33/-0.69 dB -> RT0603BRD073K3L; Manufacturer (none) -> YAGEO; SelectionNotes (none) -> 3.3k ohm notation; 0.1%; 25 ppm/K; 0603; 0.1W; 75V; SelectionStatus STUDY; passives/interfaces not selected -> MPN SELECTED; supply/DFM/bench release pending
- R601, R603: MPN 2512 thick film 1 W; MPN at BOM -> CRCW2512470RFKEG; Manufacturer (none) -> Vishay; SelectionNotes (none) -> 470; 1%; 2512; 1W; 500V; SelectionStatus STUDY; passives/interfaces not selected -> MPN SELECTED; supply/DFM/bench release pending
- R602: MPN 1206 0.25 W; 34 V max across -> CRCW120610K0FKEA; Manufacturer (none) -> Vishay; SelectionNotes (none) -> 10k; 1%; 1206; 0.25W; 200V; SelectionStatus STUDY; passives/interfaces not selected -> MPN SELECTED; supply/DFM/bench release pending
- R604: MPN 1206 0.25 W -> CRCW120610K0FKEA; Manufacturer (none) -> Vishay; SelectionNotes (none) -> 10k; 1%; 1206; 0.25W; 200V; SelectionStatus STUDY; passives/interfaces not selected -> MPN SELECTED; supply/DFM/bench release pending
- R605: MPN 0603 1 % -> CRCW060310K0FKEA; Manufacturer (none) -> Vishay; SelectionNotes (none) -> 10k; 1%; 0603; 0.1W; 75V; SelectionStatus STUDY; passives/interfaces not selected -> MPN SELECTED; supply/DFM/bench release pending
- R701: MPN SMD:R 1 % -> CRCW120647K0FKEA; Manufacturer (none) -> Vishay; SelectionNotes (none) -> 47k; 1%; 1206; 0.25W; 200V; SelectionStatus STUDY; passives/interfaces not selected -> MPN SELECTED; supply/DFM/bench release pending
- R702, R703, R704, R705, R706: MPN SMD:R 1 % -> CRCW08052K20FKEA; Manufacturer (none) -> Vishay; SelectionNotes (none) -> 2.2k; 1%; 0805; 0.125W; 150V; SelectionStatus STUDY; passives/interfaces not selected -> MPN SELECTED; supply/DFM/bench release pending
- R715, R716: MPN 0805 1 % -> CRCW080510K0FKEA; Manufacturer (none) -> Vishay; SelectionNotes (none) -> 10k; 1%; 0805; 0.125W; 150V; SelectionStatus STUDY; passives/interfaces not selected -> MPN SELECTED; supply/DFM/bench release pending
- R720: MPN 0805 1 %; fan off without jumper -> CRCW0805100KFKEA; Manufacturer (none) -> Vishay; SelectionNotes (none) -> 100k; 1%; 0805; 0.125W; 150V; SelectionStatus STUDY; passives/interfaces not selected -> MPN SELECTED; supply/DFM/bench release pending
- U1: SelectionNotes (none) -> TI SLASEA8A DDV0044D / package addendum; SelectionStatus Selected for engineering validation; NO procurement/release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 -> MPN SELECTED; supply/DFM/bench release pending
- U2, U3: Manufacturer (none) -> Texas Instruments; SelectionNotes (none) -> OPA1656ID; package and pin numbering per current native foo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; SelectionStatus CANDIDATE; NOT PULSE/ESR/POWER-OFF/FIT QUALIFIED -> MPN SELECTED; supply/DFM/bench release pending
- U302: MPN LM5164DDAR (TI SNVSAU4D Table 7-1); HSOP-8 EP footprint not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 -> LM5164DDAR; Manufacturer (none) -> Texas Instruments; SelectionNotes (none) -> LM5164DDAR (TI SNVSAU4D Table 7-1); HSOP-8 EP footprint not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; SelectionStatus STUDY; passives/interfaces not selected -> MPN SELECTED; supply/DFM/bench release pending
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
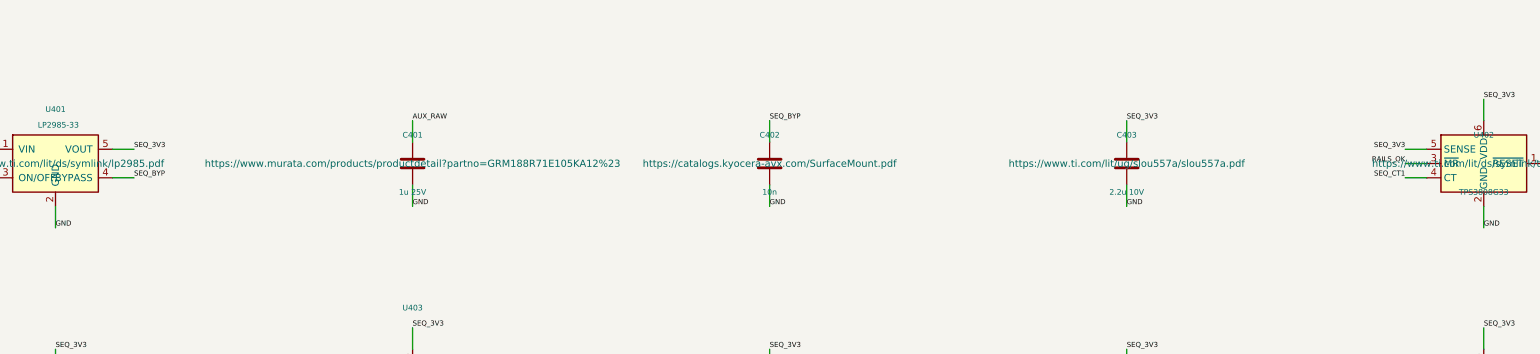
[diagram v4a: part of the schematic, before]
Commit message: fix(hardware): close SYS-002 and correct capacitor derating
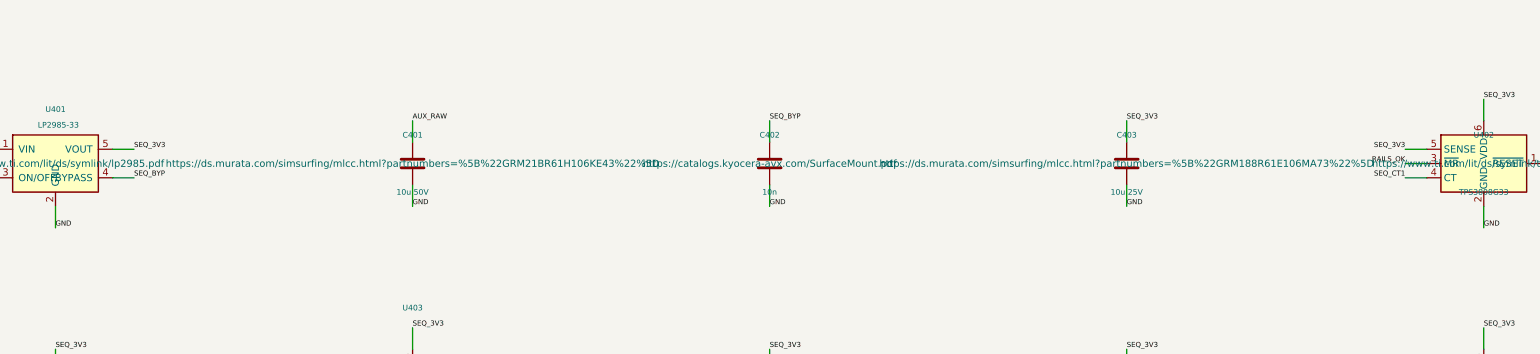
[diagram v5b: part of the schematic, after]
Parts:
- C401: value 1u 25V -> 10u 50V; footprint Capacitor_SMD:C_0603_1608Metric -> Capacitor_SMD:C_0805_2012Metric; MPN GRM188R71E105KA12D -> GRM21BR61H106KE43L; SelectionNotes 1uF; 25V; X7R; 10%; 0603; C401 input at12V: bias derating a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 -> 10uF 50V 10% X5R 0805; effective >=1uF at13.2V/10mVrms incl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; Source D-021/D-020 captures; see docs/power-d021.md and docs/seq-d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 -> https://ds.murata.com/simsurfing/mlcc.html?partnumbers=%5B%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
- C403: value 2.2u 10V -> 10u 25V; MPN GRM188Z71C225KE43D -> GRM188R61E106MA73D; SelectionNotes 2.2uF; 16V; X7R(Murata); 10%; 0603; TI EVM C118; LP2985 out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 -> 10uF 25V 20% X5R 0603; effective >=2.2uF at3.5V/10mVrms inc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; Source D-021/D-020 captures; see docs/power-d021.md and docs/seq-d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 -> https://ds.murata.com/simsurfing/mlcc.html?partnumbers=%5B%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
